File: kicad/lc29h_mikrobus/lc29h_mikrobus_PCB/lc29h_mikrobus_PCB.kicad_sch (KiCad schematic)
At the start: 45 parts, among them IC1 MIKROE-924, IC101 DS28E36BQ+U, IC102 74LVC1G3157GV,125, IC103 TXS0102DQER, J1 Conn_Coaxial, J2 Conn_01x03_Pin, Q1 DMP3013SFV, Q101 BC856B-13-F, Q102 BSS123L, Q2 NPN, SW101 SW_Nidec_CAS-120A1, U101 LC29H

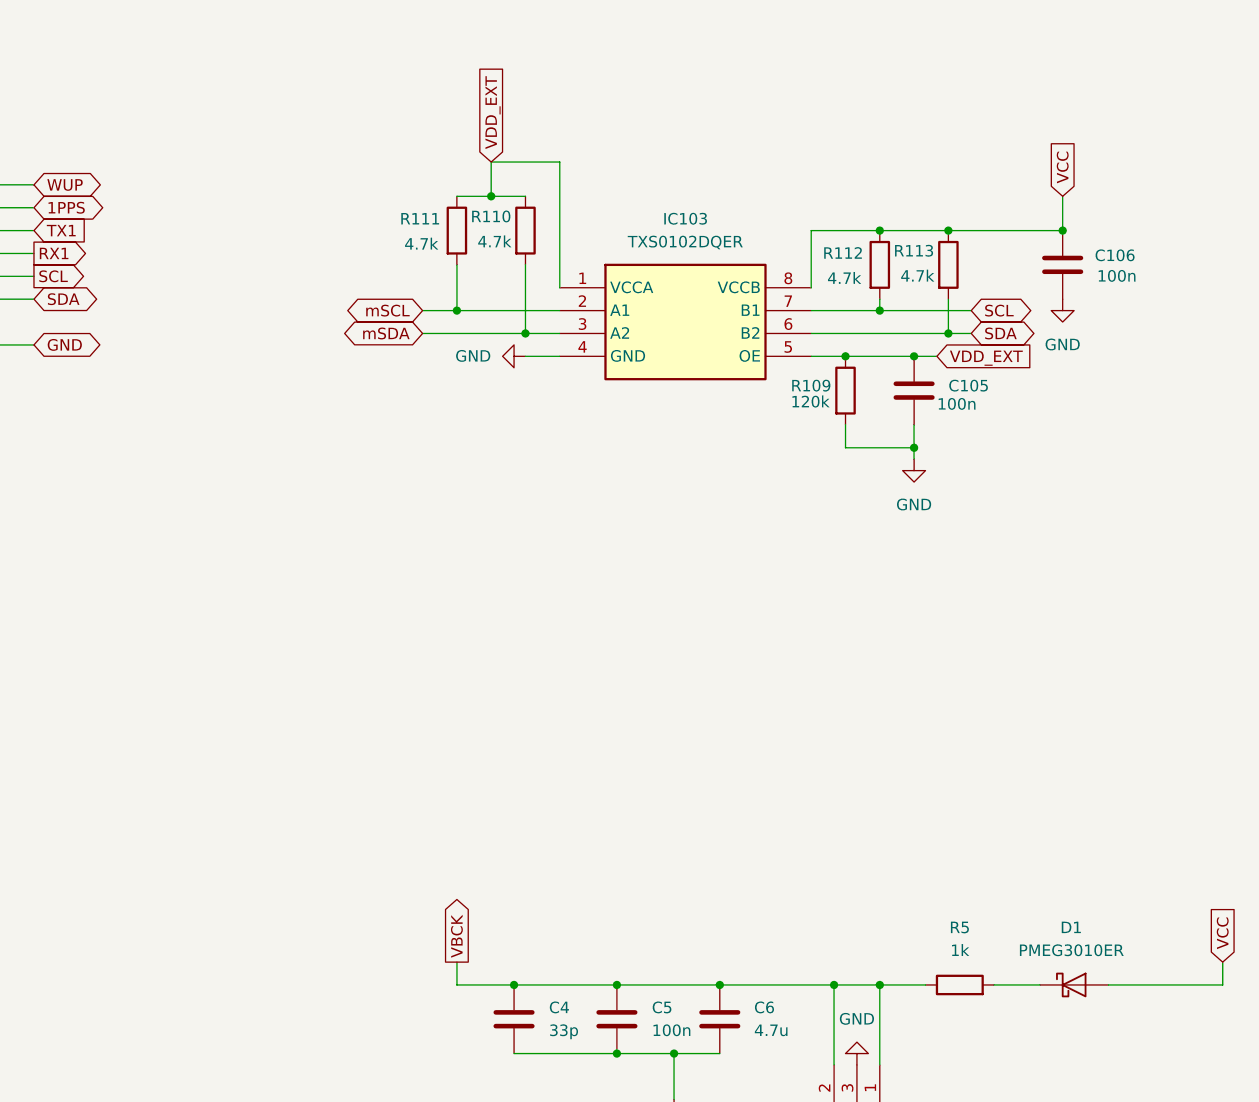
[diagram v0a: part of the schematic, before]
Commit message: Connexion PCB Composant et alimentation
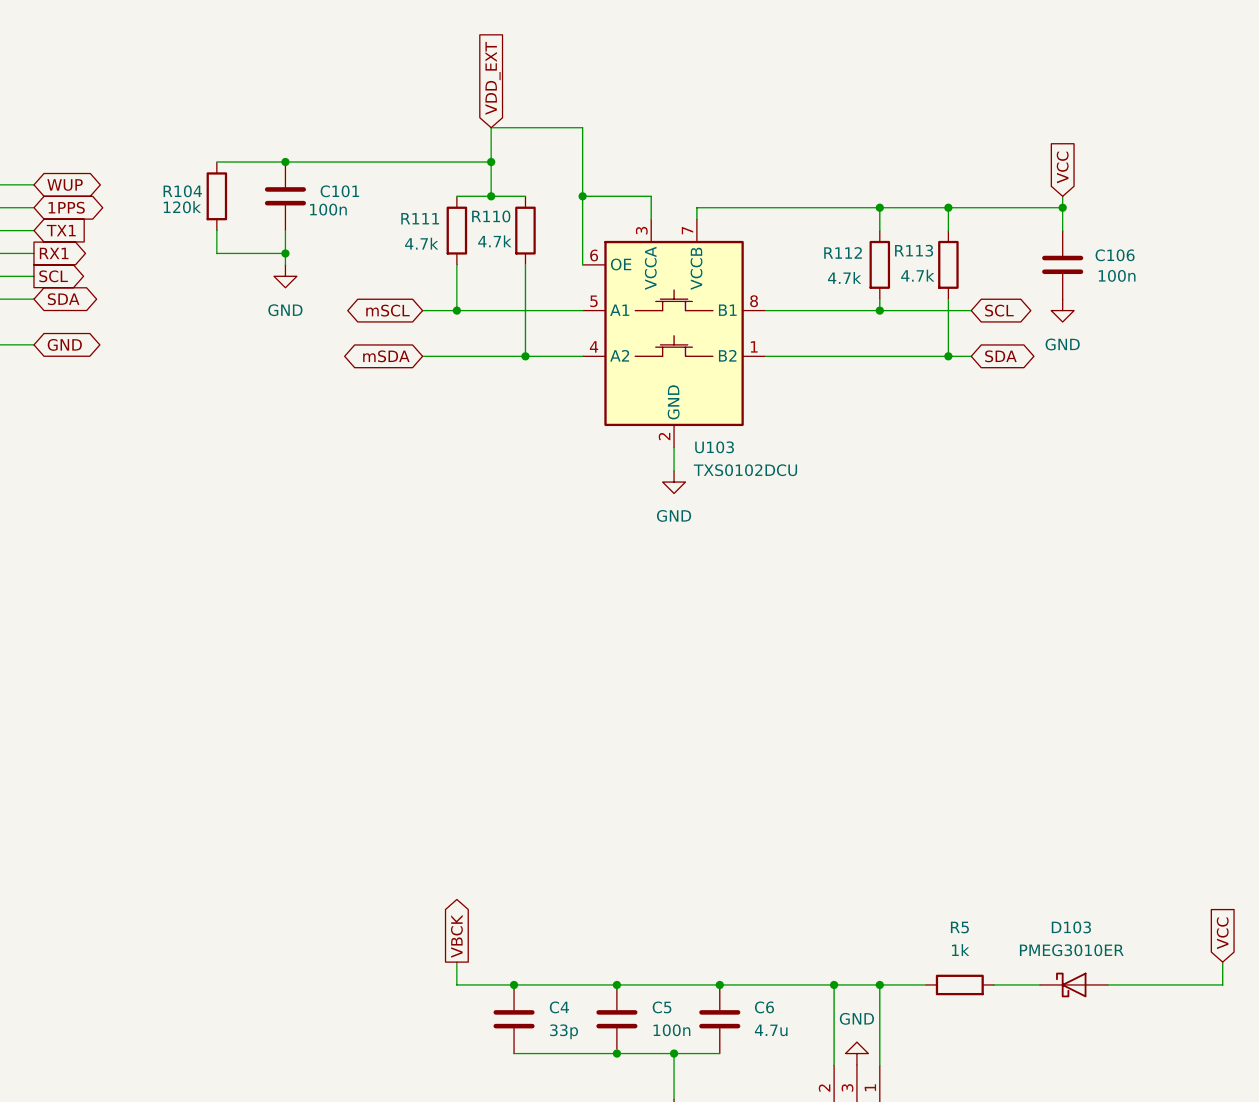
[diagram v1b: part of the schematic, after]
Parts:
- removed C105: 100n, symbol Device:C
- removed D1: PMEG3010ER, Diode_SMD:Nexperia_CFP3_SOD-123W, symbol Diode:PMEG3010ER
- removed IC103: TXS0102DQER, SON35P100X140X40-8N, symbol TXS0102DQER:TXS0102DQER
- removed R109: 120k, symbol Device:R
- added C101: 100n, Capacitor_SMD:C_0201_0603Metric, symbol Device:C
- added D103: PMEG3010ER, Diode_SMD:Nexperia_CFP3_SOD-123W, symbol Diode:PMEG3010ER
- added R104: 120k, Resistor_SMD:R_0201_0603Metric, symbol Device:R
- added U103: TXS0102DCU, Package_SO:VSSOP-8_2.3x2mm_P0.5mm, symbol Logic_LevelTranslator:TXS0102DCU
- BT1: footprint 3000TR -> 3000TR:3000TR
- C1, C104, C106, C2, C3, C4, C5, C6: footprint (none) -> Capacitor_SMD:C_0201_0603Metric
- D101: footprint (none) -> LED_SMD:LED_0402_1005Metric
- D102: footprint ESDARF021BU2CK -> ESDARF02-1BU2CK:ESDARF021BU2CK
- IC101: footprint SON95P300X300X80-7N -> DS28E36BQ+U:SON95P300X300X80-7N
- IC102: footprint SOP95P275X110-6N -> 74LVC1G3157GV_125:SOP95P275X110-6N
- L1: footprint (none) -> Inductor_SMD:L_0201_0603Metric
- Q101: footprint SOT96P240X110-3N -> BC856B-13-F:SOT96P240X110-3N
- Q102: footprint SOT96P237X111-3N -> BSS123L:SOT96P237X111-3N
- R1, R101, R102, R105, R106, R107, R108, R110, R111, R112, R113, R114, R115, R2, R5: footprint (none) -> Resistor_SMD:R_0201_0603Metric
- R103: footprint (none) -> Resistor_SMD:R_0603_1608Metric_Pad0.98x0.95mm_HandSolder
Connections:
- net GND: now also C101.2, R104.2, U103.2 (GND)
- net SCL: now also U103.8 (B1)
- net SDA: now also U103.1 (B2)
- net VCC: now also D103.2 (A), U103.7 (VCCB)
- net VDD_EXT: now also C101.1, R104.1, U103.3 (VCCA), U103.6 (OE)
- net mSCL: now also U103.5 (A1)
- net mSDA: now also U103.4 (A2)
- net at R5.2: now also D103.1 (K)

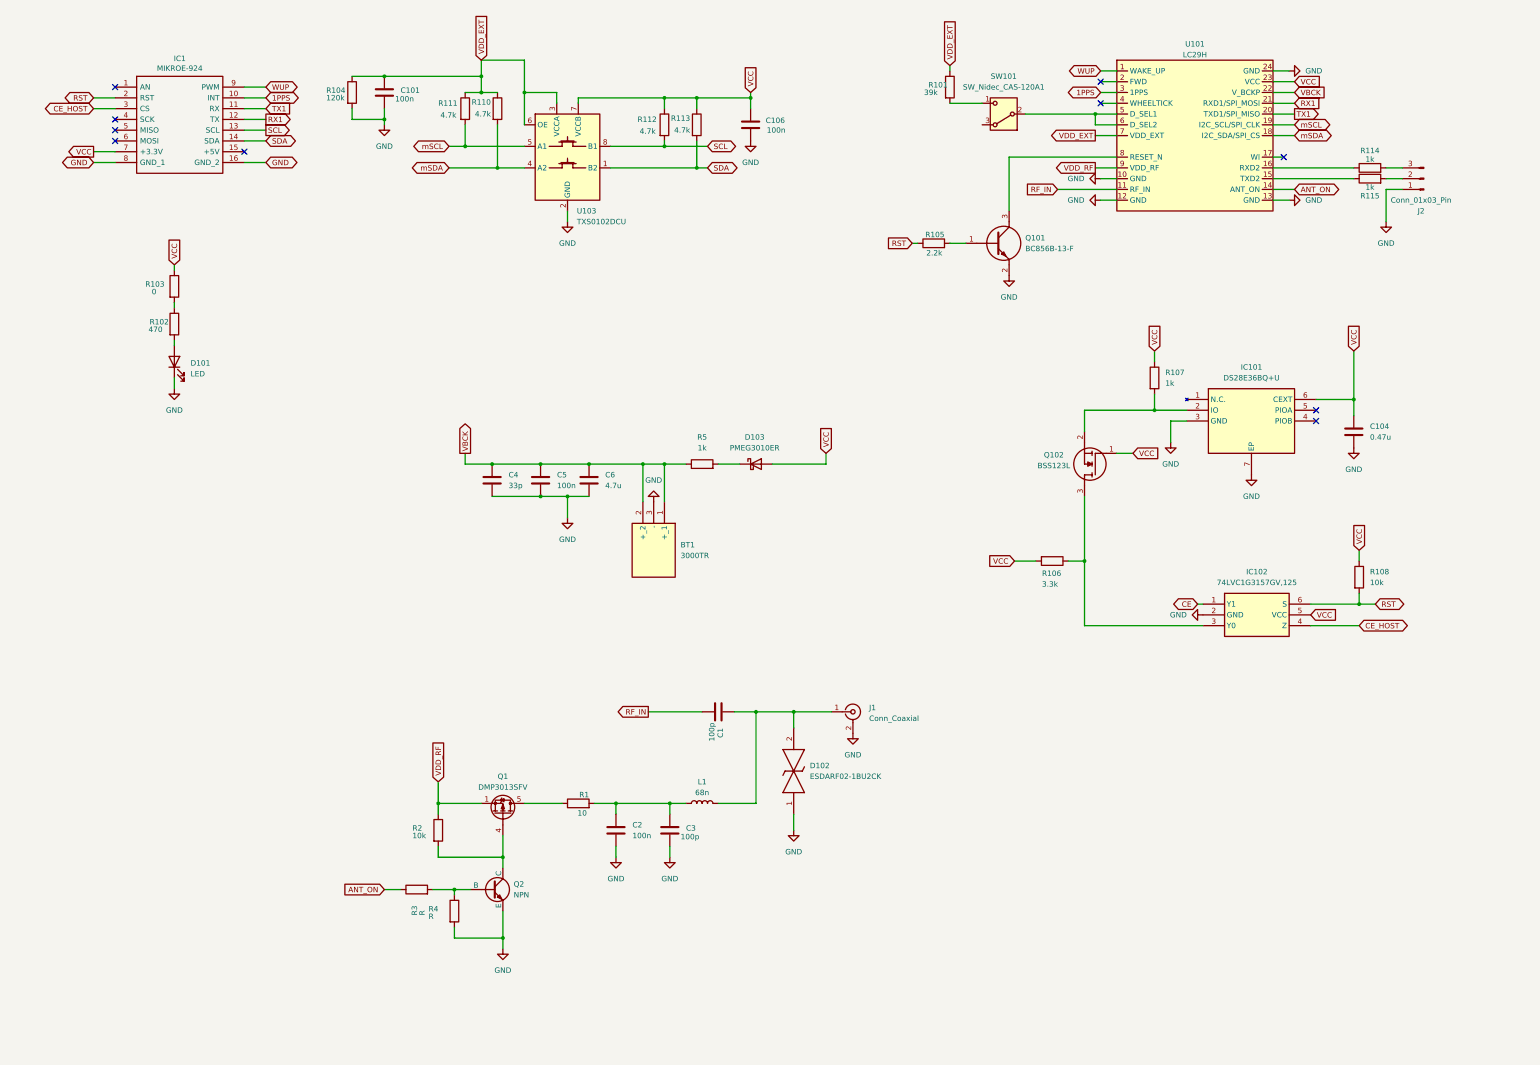
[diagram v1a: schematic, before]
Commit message: association de toutes les empreintes et début de la finalisation du routage
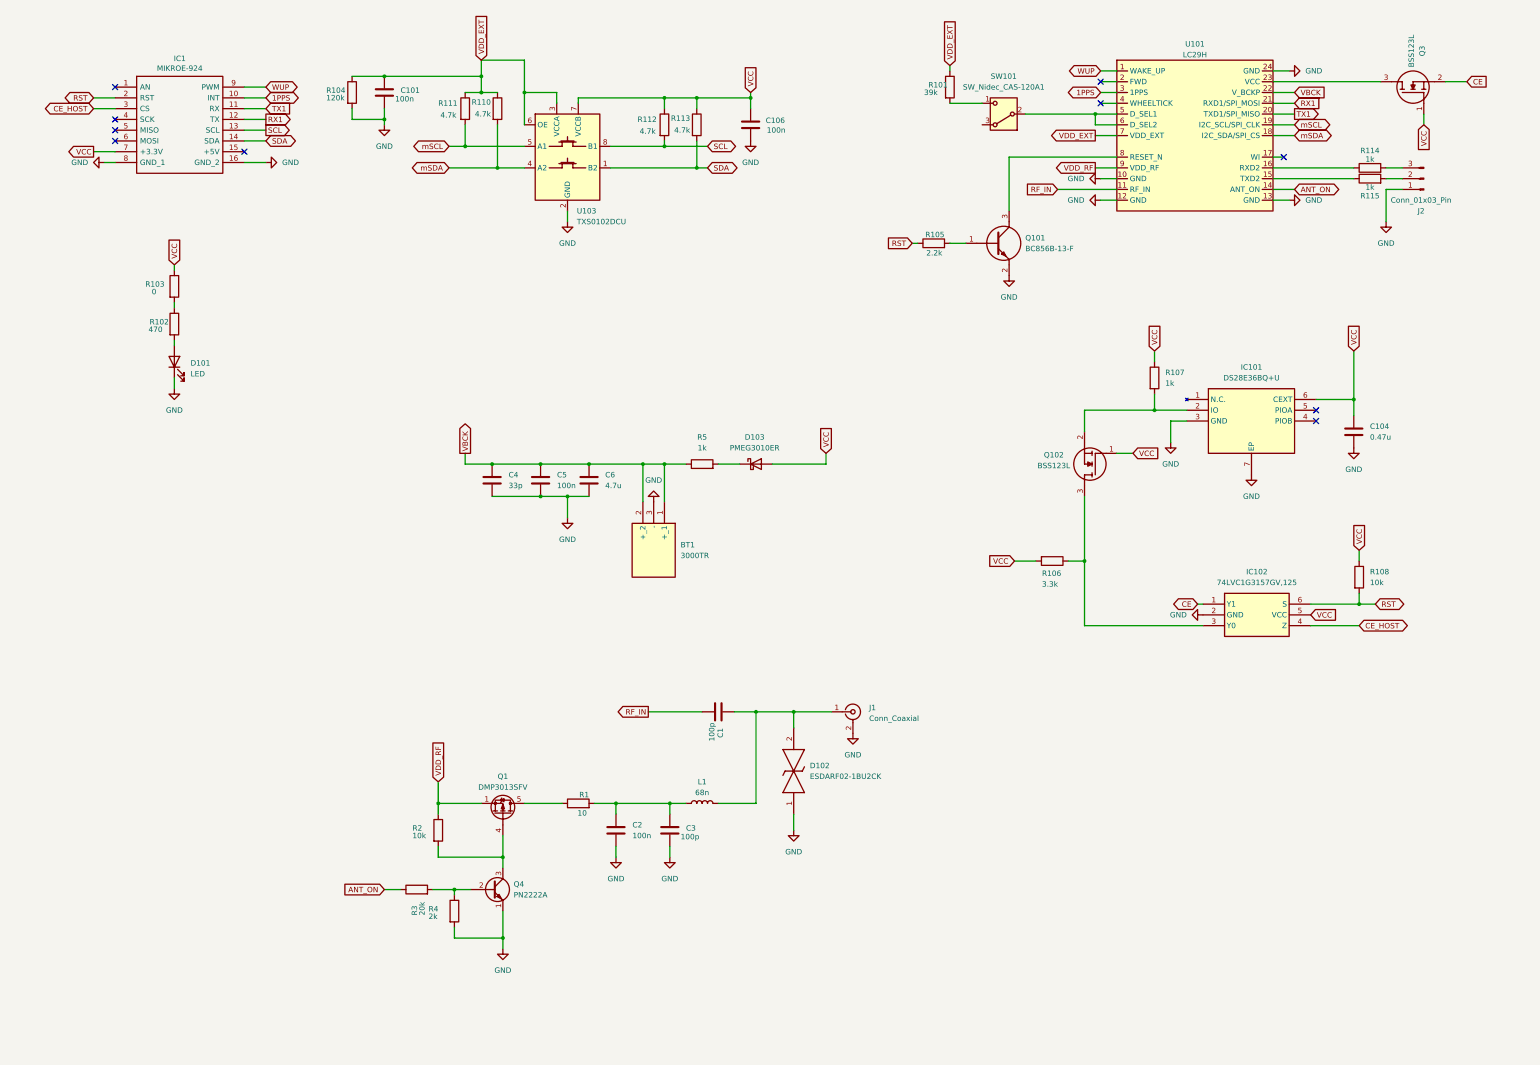
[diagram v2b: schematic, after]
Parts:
- removed Q2: NPN, symbol Simulation_SPICE:NPN
- added Q3: BSS123L, BSS123L:SOT96P237X111-3N, symbol BSS123L:BSS123L
- added Q4: PN2222A, Package_TO_SOT_THT:TO-92_Inline, symbol Transistor_BJT:PN2222A
- J1: footprint (none) -> Connector_Coaxial:SMA_Amphenol_901-144_Vertical
- J2: footprint (none) -> Connector_PinHeader_1.27mm:PinHeader_1x03_P1.27mm_Vertical
- R3: value R -> 20k; footprint (none) -> Resistor_SMD:R_0201_0603Metric
- R4: value R -> 2k; footprint (none) -> Resistor_SMD:R_0201_0603Metric
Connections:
- net CE: now also Q3.2 (S)
- net GND: now also Q4.1 (E)
- net VCC: now also Q3.1 (G); no longer U101.23 (VCC)
- net at Q1.4 (G), R2.2: now also Q4.3 (C)
- net at R3.2, R4.1: now also Q4.2 (B)
- new net: Q3.3 (D), U101.23 (VCC)
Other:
- title: (none) -> lc29h_mikrobus V1

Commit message: add attributes
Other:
- company: (none) -> (c) 2024 - Université Grenoble Alpes - Grenoble INP - LIG + CSUG
- title: lc29h_mikrobus V1 -> Quectel LC29H Mikrobus V1
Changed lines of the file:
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@@
 	(paper "A3")
 	(title_block
-		(title "lc29h_mikrobus V1")
+		(title "Quectel LC29H Mikrobus V1")
 		(date "01/07/2024")
+		(company "(c) 2024 - Université Grenoble Alpes - Grenoble INP - LIG + CSUG")
+		(comment 1 "Author : Jihane ZEMMOURA")
 	)
 	(junction

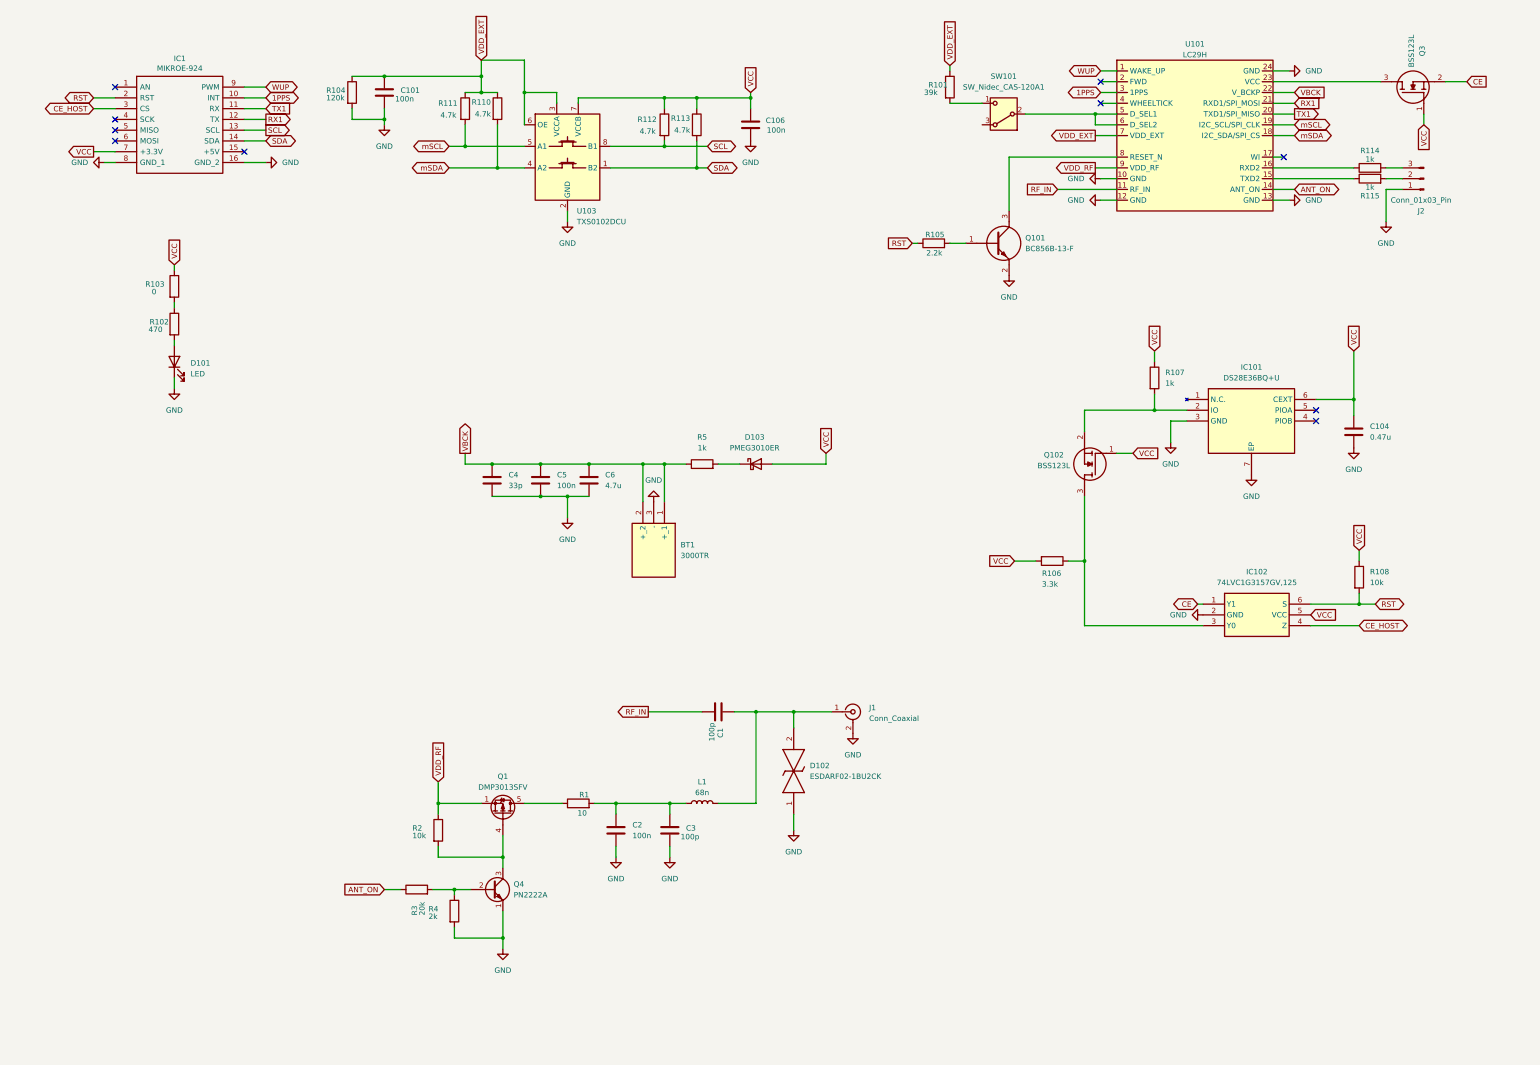
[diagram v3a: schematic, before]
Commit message: rearrange components and remove most warnings
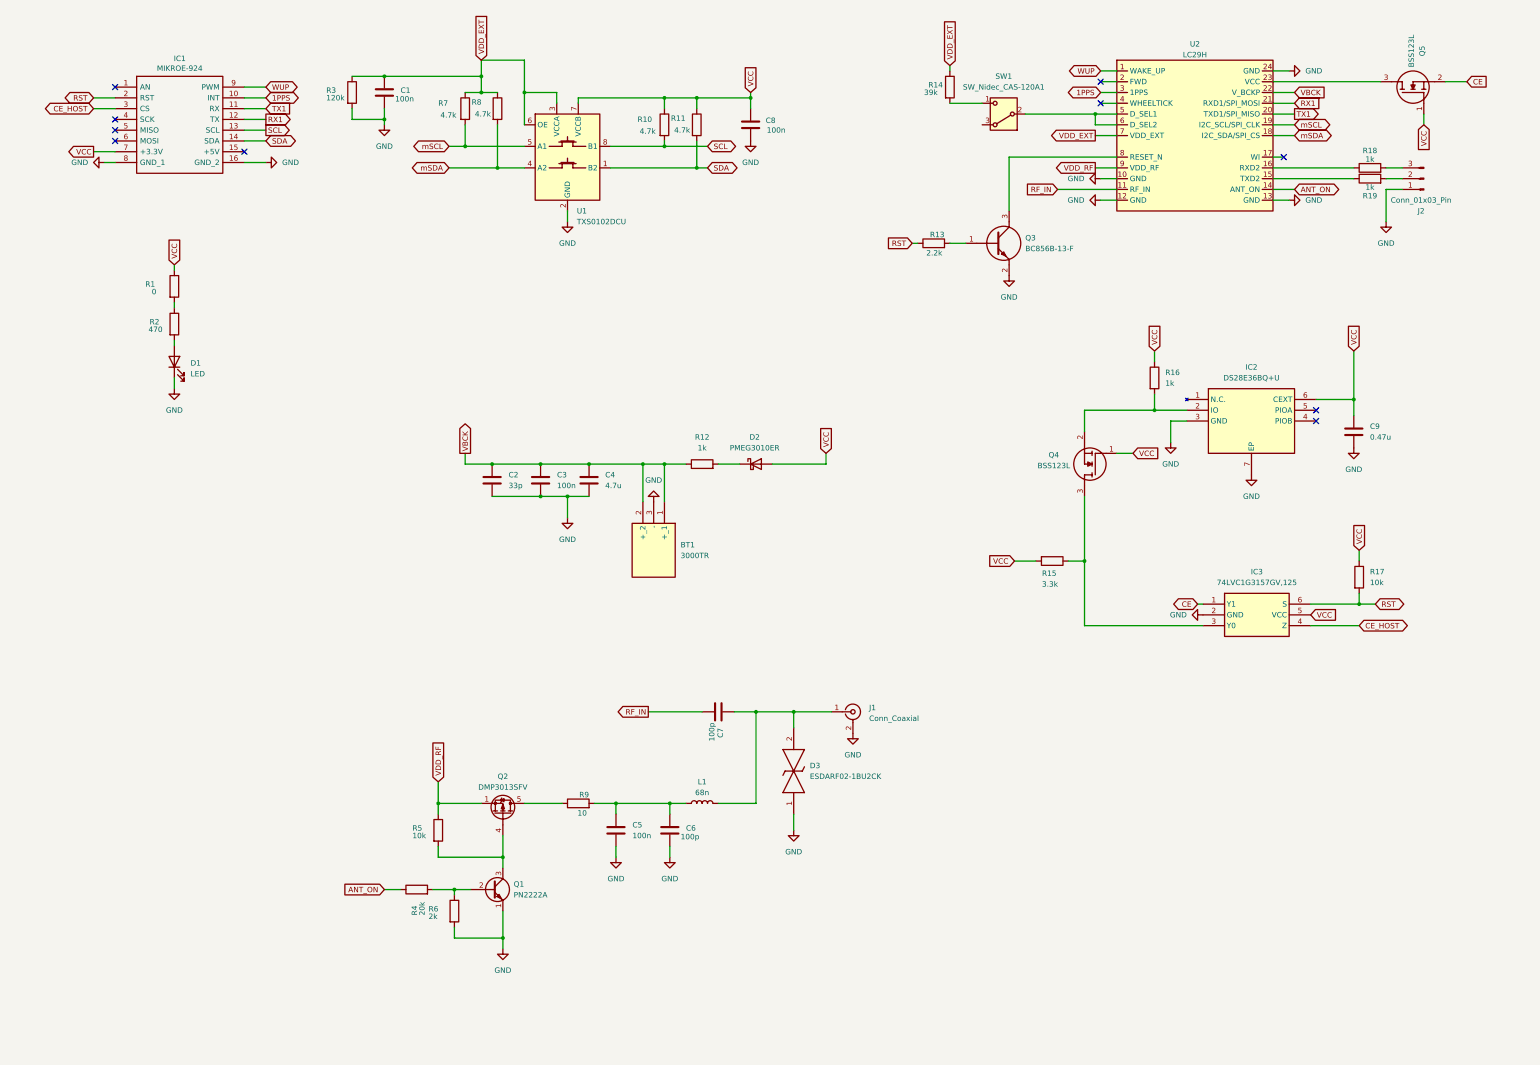
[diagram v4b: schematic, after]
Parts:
- renumbered C101 to C1, C4 to C2, C5 to C3, C6 to C4, C2 to C5, C3 to C6, C1 to C7, C106 to C8, C104 to C9, D101 to D1, D103 to D2, D102 to D3, IC101 to IC2, IC102 to IC3, Q4 to Q1, Q1 to Q2, Q101 to Q3, Q102 to Q4, Q3 to Q5, R103 to R1, R112 to R10, R113 to R11, R5 to R12, R105 to R13, R101 to R14, R106 to R15, R107 to R16, R108 to R17, R114 to R18, R115 to R19, R102 to R2, R104 to R3, R3 to R4, R2 to R5, R4 to R6, R111 to R7, R110 to R8, R1 to R9, SW101 to SW1, U103 to U1, U101 to U2
